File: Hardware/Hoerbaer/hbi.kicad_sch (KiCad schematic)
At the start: 49 parts, among them J6 PAW_A, J7 PAW_B, J8 PAW_C, J9 PAW_D, U2 PCF8574APWR, U3 PCF8574APWR, U4 PCF8574APWR, U5 TLC59108xPW, U6 TLC59108xPW, U7 TLC59108xPW

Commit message: Many small corrections, changed connectors, ...
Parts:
- J6, J7, J8, J9: now not fitted
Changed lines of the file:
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@@
   )
   (symbol (lib_id "Connector_Generic:Conn_02x12_Odd_Even") (at 72.39 139.7 0) (unit 1)
-    (in_bom yes) (on_board yes) (dnp no)
+    (in_bom yes) (on_board yes) (dnp yes)
     (property "Reference" "J9" (at 73.66 121.92 0)
       (effects (font (size 1.27 1.27)))
@@
   )
   (symbol (lib_id "Connector_Generic:Conn_02x12_Odd_Even") (at 72.39 96.52 0) (unit 1)
-    (in_bom yes) (on_board yes) (dnp no)
+    (in_bom yes) (on_board yes) (dnp yes)
     (property "Reference" "J8" (at 73.66 78.74 0)
       (effects (font (size 1.27 1.27)))
@@
   )
   (symbol (lib_id "Connector_Generic:Conn_02x12_Odd_Even") (at 36.83 96.52 0) (unit 1)
-    (in_bom yes) (on_board yes) (dnp no)
+    (in_bom yes) (on_board yes) (dnp yes)
     (property "Reference" "J6" (at 38.1 78.74 0)
       (effects (font (size 1.27 1.27)))
@@
   )
   (symbol (lib_id "Connector_Generic:Conn_02x12_Odd_Even") (at 36.83 139.7 0) (unit 1)
-    (in_bom yes) (on_board yes) (dnp no)
+    (in_bom yes) (on_board yes) (dnp yes)
     (property "Reference" "J7" (at 38.1 121.92 0)
       (effects (font (size 1.27 1.27)))

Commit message: WIP new hw rev
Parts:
- renumbered C23 to C10, C6 to C11, C7 to C12, C8 to C13, C9 to C14, C10 to C15, C11 to C16, C22 to C7, C65 to C8, C24 to C9, J8 to J10, J9 to J11, J6 to J8, J7 to J9
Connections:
- net +12V renamed +9V
- net VCC renamed VCC_P

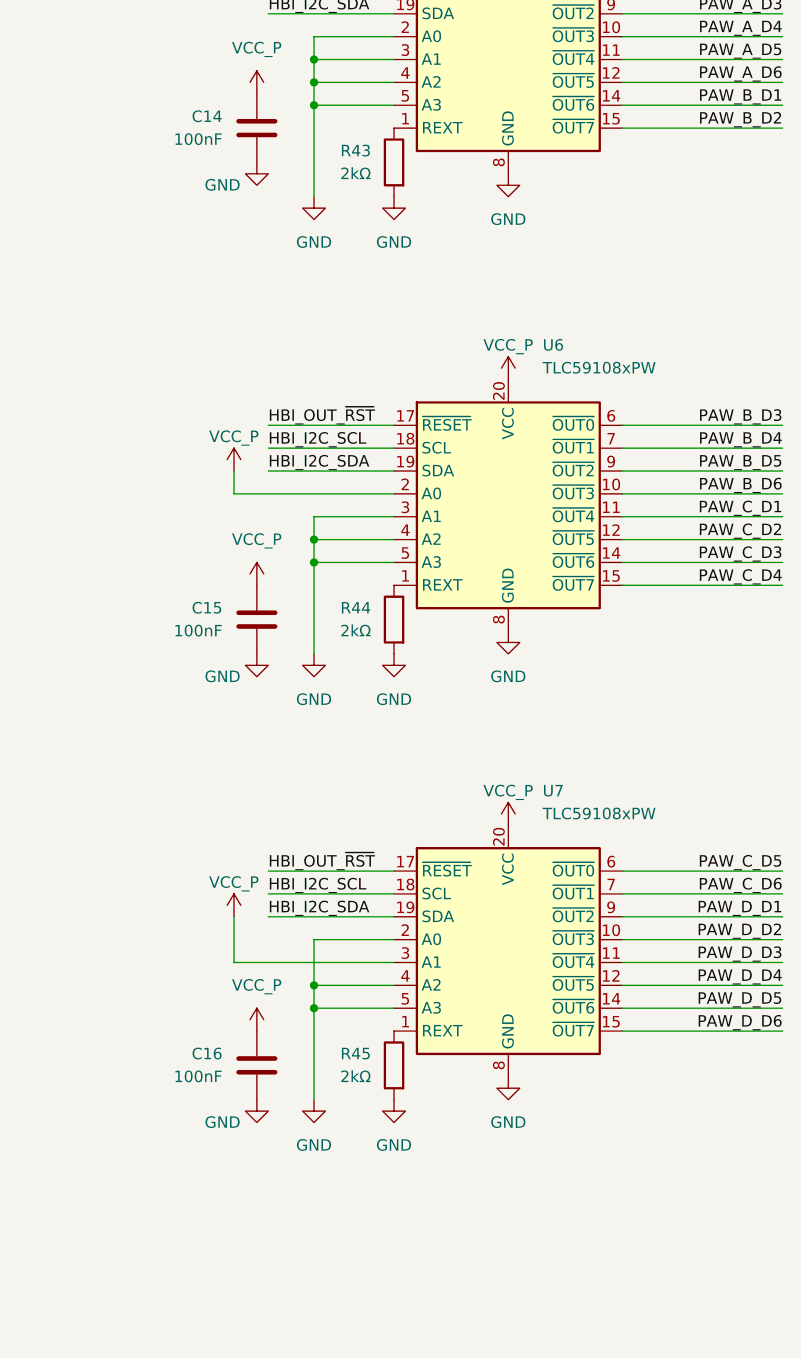
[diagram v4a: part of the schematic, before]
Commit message: Added more jumper options.
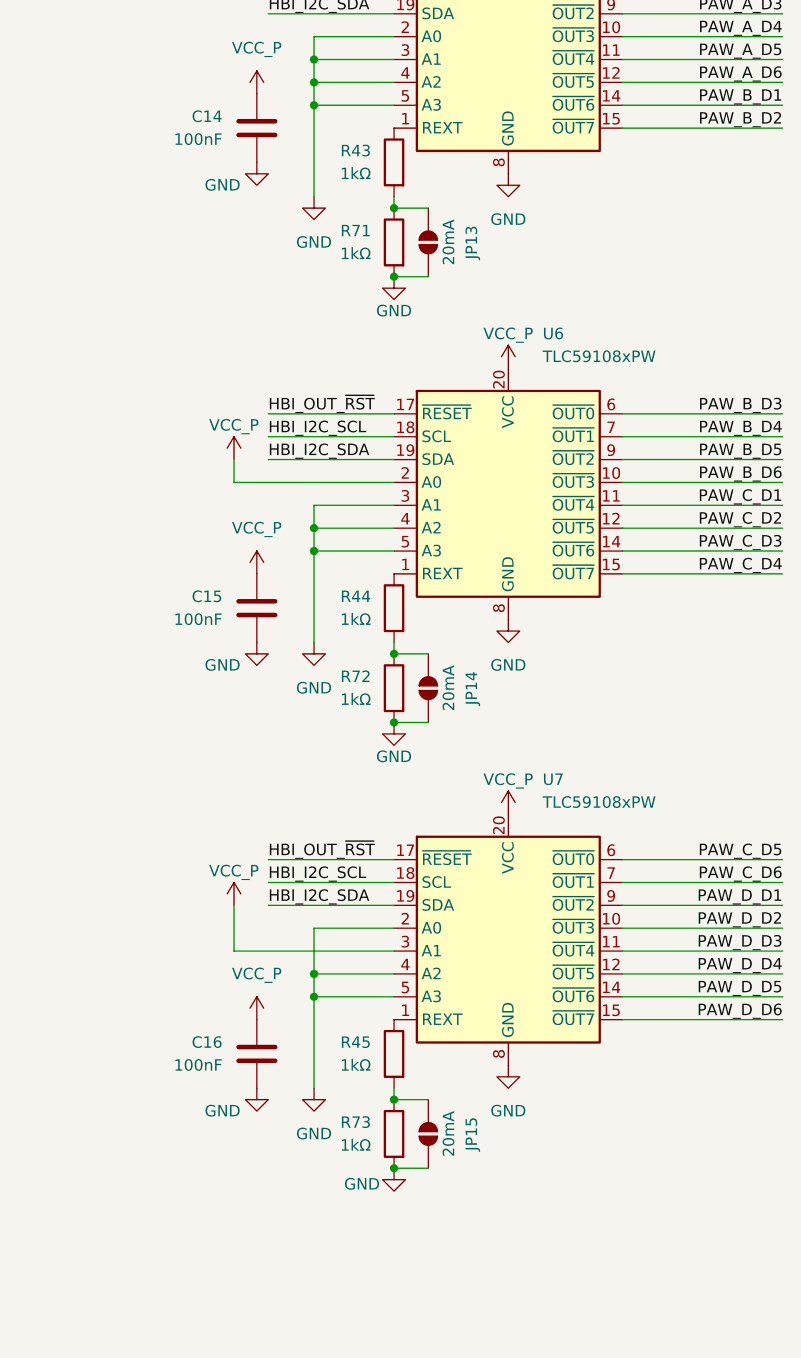
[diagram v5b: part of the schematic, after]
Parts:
- added JP13, JP14, JP15: 20mA, Jumper:SolderJumper-2_P1.3mm_Open_RoundedPad1.0x1.5mm, symbol Jumper:SolderJumper_2_Open
- added R71, R72, R73: 1kΩ, Resistor_SMD:R_0402_1005Metric, symbol Device:R
- R43, R44, R45: value 2kΩ -> 1kΩ; LCSC C4109 -> C11702; MPN 0402WGF2001TCE -> 0402WGF1001TCE
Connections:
- net GND: now also JP13.2 (B), JP14.2 (B), JP15.2 (B), R71.2, R72.2, R73.2; no longer R43.2, R44.2, R45.2
- new net: JP14.1 (A), R44.2, R72.1
- new net: JP13.1 (A), R43.2, R71.1
- new net: JP15.1 (A), R45.2, R73.1
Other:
- moved on the sheet: C15, C16, U6, U7

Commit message: BOM FIxes
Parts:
- C11, C12, C13, C14, C15, C16: LCSC C458949 -> C1525; MPN MT15B104K160CT -> CL05B104KO5NNNC
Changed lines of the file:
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@@
 			"L0RvY3VtZW50RGVsaXZlcnkvRERFQ29udHJvbGxlcj9BY3Rpb249c3JjaHJ0cnYmRG9jTm09ODI2"
 			"NTc2JkRvY1R5cGU9Q3VzdG9tZXIrRHJhd2luZyZEb2NMYW5nPUVuZ2xpc2gpLCBnZW5lcmF0ZWQg"
-			"d2l0aCBraWNhZC1mb290cA=="
+			"d2l0aCBraWNhZC1mb290cEggcGl0Y2ggMy41bW0gc2l6ZSA1Nng3LjZtbSBkcmlsbCAxLjJtbSBw"
+			"YWQgMi40bW0KMAoxNgoxNgpUZXJtaW5hbEJsb2NrX1Bob2VuaXgKVGVybWluYWxCbG9ja19QaG9l"
+			"bml4X1BULTEsNS0xNi01LjAtSF8xeDE2X1A1LjAwbW1fSG9yaXpvbnRhbApUZXJtaW5hbCBCbG9j"
+			"ayBQaG9lbml4IFBULTEsNS0xNi01LjAtSCwgMTYgcGlucywgcGl0Y2ggNW1tLCBzaXplIDgweDlt"
+			"bSwgZHJpbGwgZGlhbWV0ZXIgMS4zbW0sIHBhZCBkaWFtZXRlciAyLjZtbSwgaHR0cDovL3d3dy5t"
+			"b3VzZXIuY29tL2RzLzIvMzI0L0l0ZW1EZXRhaWxfMTkzNTE2MS05MjI1NzgucGRmLCBzY3JpcHQt"
+			"Z2VuZXJhdGVkIHVzaW5nIGh0dHBzOi8vZ2l0bGFiLmNvbS9raWNhZC9saWJyYXJpZXMva2ljYWQt"
+			"Zm9vdHByaW50LWdlbmVyYXRvci8tL3RyZWUvbWFzdGVyL3NjcmlwdHMvVGVybWluYWxCbG9ja19Q"
+			"aG9lbml4ClRIVCBUZXJtaW5hbCBCbG9jayBQaG9lbml4IFBULTEsNS0xNi01LjAtSCBwaXRjaCA1"
+			"bW0gc2l6ZSA4MHg5bW0gZHJpbGwgMS4zbW0gcGFkIDIuNm1tCjAKMTYKMTYKVGVybWluYWxCbG9j"
+			"a19QaG9lbml4ClRlcm1pbmFsQmxvY2tfUGhvZW5peF9QVFNNLTAsNS0yLTIsNS1WLVNNRF8xeDAy"
+			"LTFNUF9QMi41MG1tX1ZlcnRpY2FsClBob2VuaXhDb250YWN0IFBUU00wLDUgMiAyLDVtbSB2ZXJ0"
+			"aWNhbCBTTUQgc3ByaW5nIGNsYW1wIHRlcm1pbmFsIGJsb2NrIGNvbm5lY3RvciBodHRwOi8vd3d3"
+			"LnBob2VuaXhjb250YWN0LmNvbS91cy9wcm9kdWN0cy8xODE0NzAyL3BkZgpQaG9lbml4Q29udGFj"
+			"dCBQVFNNMC41IDIgMi41bW0gdmVydGljYWwgU01EIHNwcmluZyBjbGFtcCB0ZXJtaW5hbCBibG9j"
+			"ayBjb25uZWN0b3IgCjAKNAozClRlcm1pbmFsQmxvY2tfUGhvZW5peApUZXJtaW5hbEJsb2NrX1Bo"
+			"b2VuaXhfUFRTTS0wLDUtMi0yLjUtSC1USFJfMXgwMl9QMi41MG1tX0hvcml6b250YWwKVGVybWlu"
+			"YWwgQmxvY2sgUGhvZW5peCBQVFNNLTAsNS0yLTIuNS1ILVRIUiwgMiBwaW5zLCBwaXRjaCAyLjVt"
+			"bSwgc2l6ZSA3LjJ4MTBtbQ=="
 		)
 	)
@@
 			)
 		)
-		(property "LCSC" "C458949"
+		(property "LCSC" "C1525"
 			(at 99.06 110.49 0)
 			(effects
@@
 			)
 		)
-		(property "MPN" "MT15B104K160CT"
+		(property "MPN" "CL05B104KO5NNNC"
 			(at 99.06 110.49 0)
 			(effects
@@
 			)
 		)
-		(property "LCSC" "C458949"
+		(property "LCSC" "C1525"
 			(at 214.63 46.99 0)
 			(effects
@@
 			)
 		)
-		(property "MPN" "MT15B104K160CT"
+		(property "MPN" "CL05B104KO5NNNC"
 			(at 214.63 46.99 0)
 			(effects
@@
 			)
 		)
-		(property "LCSC" "C458949"
+		(property "LCSC" "C1525"
 			(at 99.06 48.26 0)
 			(effects
@@
 			)
 		)
-		(property "MPN" "MT15B104K160CT"
+		(property "MPN" "CL05B104KO5NNNC"
 			(at 99.06 48.26 0)
 			(effects
@@
 			)
 		)
-		(property "LCSC" "C458949"
+		(property "LCSC" "C1525"
 			(at 214.63 149.86 0)
 			(effects
@@
 			)
 		)
-		(property "MPN" "MT15B104K160CT"
+		(property "MPN" "CL05B104KO5NNNC"
 			(at 214.63 149.86 0)
 			(effects
@@
 			)
 		)
-		(property "LCSC" "C458949"
+		(property "LCSC" "C1525"
 			(at 99.06 170.18 0)
 			(effects
@@
 			)
 		)
-		(property "MPN" "MT15B104K160CT"
+		(property "MPN" "CL05B104KO5NNNC"
 			(at 99.06 170.18 0)
 			(effects
@@
 			)
 		)
-		(property "LCSC" "C458949"
+		(property "LCSC" "C1525"
 			(at 214.63 100.33 0)
 			(effects
@@
 			)
 		)
-		(property "MPN" "MT15B104K160CT"
+		(property "MPN" "CL05B104KO5NNNC"
 			(at 214.63 100.33 0)
 			(effects

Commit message: Production
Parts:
- J10, J11, J8, J9: FT Rotation Offset (none) -> 90; JLCPCB Rotation Offset 90 -> (none)
- U2, U3, U4, U5, U6, U7: JLCPCB Rotation Offset 90 -> (none)
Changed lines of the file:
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@@
 			"b2VuaXhfUFRTTS0wLDUtMi0yLjUtSC1USFJfMXgwMl9QMi41MG1tX0hvcml6b250YWwKVGVybWlu"
 			"YWwgQmxvY2sgUGhvZW5peCBQVFNNLTAsNS0yLTIuNS1ILVRIUiwgMiBwaW5zLCBwaXRjaCAyLjVt"
-			"bSwgc2l6ZSA3LjJ4MTBtbQ=="
+			"bSwgc2l6ZSA3LjJ4MTBtbf//////////////////////////////////////////////////////"
+			"////////////////////////////////////////////////////////////////////////////"
+			"////////////////////////////////////////////////////////////////////////////"
+			"////////////////////////////////////////////////////////////////////////////"
+			"////////////////////////////////////////////////////////////////////////////"
+			"////////////////////////////////////////////////////////////////////////////"
+			"////////////////////////////////////////////////////////////////////////////"
+			"////////////////////////////////////////////////////////////////////////////"
+			"////////////////////////////////////////////////////////////////////////////"
+			"////////////////////////////////////////////////////////////////////////////"
+			"////////////////////////////////////////////////////////////////////////////"
+			"////////////////////////////////////////////////////////////////////////////"
+			"////////////////////////////////////////////////////////////////////////////"
+			"////////////////////////////////////////////////////////////////////////////"
+			"////////////////////////////////////////////////////////////////////////////"
+			"////////////////////////////////////////////////////////////////////////////"
+			"////////////////////////////////////////////////////////////////////////////"
+			"////////////////////////////////////////////////////////////////////////////"
+			"/////////////////////4guiC6ILoguiC6ILoguiC6ILoguiC6ILoguiC6ILoguiC6ILoguiC6I"
+			"LoguiC6ILoguiC6ILoguiC6ILoguiC6ILoguiC6ILoguiC6ILoguiC6ILoguiC6ILoguiC6ILogu"
+			"iC6ILoguiC6ILoguiC6ILoguiC6ILoguiC6ILoguiC6ILoguiC6ILoguiC6ILoguiC6ILoguiC6I"
+			"LoguiC6ILoguiC6ILoguiC6ILoguiC6ILoguiC6ILoguiC6ILoguiC6ILoguiC6ILoguiC6ILogu"
+			"iC6ILoguiC6ILoguiC6ILoguiC6ILoguiC6ILoguiC6ILoguiC6ILoguiC6ILoguiC6ILoguiC6I"
+			"LoguiC6ILoguiC6ILoguiC6ILoguiC6ILoguiC6ILoguiC6ILoguiC6ILoguiC6ILoguiC6ILogu"
+			"iC6ILoguiC6ILoguiC6ILoguiC6ILoguiC6ILoguiC6ILoguiC6ILoguiC6ILoguiC6ILoguiC6I"
+			"LoguiC6ILoguiC6ILoguiC6ILoguiC6ILoguiC6ILoguiC6ILoguiC6ILoguiC6ILoguiC6ILogu"
+			"iC6ILoguiC6ILoguiC6ILoguiC6ILoguiC6ILoguiC6ILoguiC6ILoguiC6ILoguiC6ILoguiC6I"
+			"LoguiC6ILoguiC6ILoguiC6ILoguiC6ILoguiC6ILoguiC6ILoguiC6ILoguiC6ILoguiC6ILogu"
+			"iC6ILoguiC6ILoguiC6ILoguiC6ILoguiC6ILoguiC6ILoguiC6ILoguiC6ILoguiC6ILoguiC6I"
+			"LoguiC6ILoguiC6ILoguiC6ILoguiC6ILoguiC6ILoguiC6ILoguiC6ILoguiC6ILoguiC6ILogu"
+			"iC6ILoguiC6ILoguiC6ILoguiC6ILoguiC6ILoguiC6ILoguiC6ILoguiC6ILoguiC6ILoguiC6I"
+			"LoguiC6ILoguiC6ILoguiC6ILoguiC6ILoguiC6ILoguiC6ILoguiC6ILoguiC6ILoguiC6ILogu"
+			"iC6ILoguiC6ILoguiC6ILoguiC6ILoguiC6ILoguiC6ILoguiC6ILoguiC6ILoguiC6ILoguiC6I"
+			"LoguiC6ILoguiC6ILoguiC6ILoguiC6ILoguiC6ILoguiC6ILoguiC6ILoguiC6ILoguiC6ILogu"
+			"iC6ILoguiC6ILoguiC6ILoguiC6ILoguiC6ILoguiC6ILoguiC6ILoguiC6ILoguiC6ILoguiC6I"
+			"LoguiC6ILoguiC6ILoguiC6ILoguiC6ILoguiC6ILoguiC6ILoguiC6ILoguiC6ILoguiC6ILogu"
+			"iC6ILoguiC6ILoguiC6ILgAAAAAAAAAAAAAAAAAAAAAAAAAAAAAAAAAAAAAAAAAAAAAAAAAAAAAA"
+			"AAAAAAAAAAAAAAAAAAAAAAAAAAAAAAAAAAAAAAAAAAAAAAAAAAAAAAAAAAAAAAAAAAAAAAAAAAAA"
+			"AAAAAAAAAAAAAAAAAAAAAAAAAAAAAAAAAAAAAAAAAAAAAAAAAAAAAAAAAAAAAAAAAAAAAAAAAAAA"
+			"AAAAAAAAAAAAAAAAAAAAAAAAAAAAAAAAAAAAAAAAAAAAAAAAAAAAAAAAAAAAAAAAAAAAAAAAAAAA"
+			"AAAAAAAAAAAAAAAAAAAAAAAAAAAAAAAAAAAAAAAAAAAAAAAAAAAAAAAAAAAAAAAAAAAAAAAAAAAA"
+			"AAAAAAAAAAAAAAAAAAAAAAAAAAAAAAAAAAAAAAAAAAAAAAAAAAAAAAAAAAAAAAAAAAAAAAAAAAAA"
+			"AAAAAAAAAAAAAAAAAAAAAAAAAAAAAAAAAAAAAAAAAAAAAAAAAAAAAAAAAAAAAAAAAAAAAAAAAAAA"
+			"AAAAAAAAAAAAAAAAAAAAAAAAAAAAAAAAAAAAAAAAAAAAAAAAAAAAAAAAAAAAAAAAAAAAAAAAAAAA"
+			"AAAAAAAAAAAAAAAAAAAAAAAAAAAAAAAAAAAAAAAAAAAAAAAAAAAAAAAAAAAAAAAAAAAAAAAAAAAA"
+			"AAAAAAAAAAAAAAAAAAAAAAAAAAAAAAAAAAAAAAAAAAAAAAAAAAAAAAAAAAAAAAAAAAAAAAAAAAAA"
+			"AAAAAAAAAAAAAAAAAAAAAAAAAAAAAAAAAAAAAAAAAAAAAAAAAAAAAAAAAAAAAAAAAAAAAAAAAAAA"
+			"AAAAAAAAAAAAAAAAAAAAAAAAAAAAAAAAAAAAAAAAAAAAAAAAAAAAAAAAAAAAAAAAAAAAAAAAAAAA"
+			"AAAAAAAAAAAAAAAAAAAAAAAAAAAAAAAAAAAAAAAAAAAAAAAAAAAAAAAAAAAAAAAAAAAAAAAAAAAA"
+			"AAAAAAAAAAAAAAAAAAAAAAAAAAAAAAAAAAAAAAAAAAAAAAAAAAAAAAAAAAAAAAAAAAAAAAAAAAAA"
+			"AAAAAAAAAAAAAAAAAAAAAAAAAAAAAAAAAAAAAAAAAAAAAAAAAAAAAAAAAAAAAAAAAAAAAAAAAAAA"
+			"AAAAAAAAAAAAAAAAAAAAAAAAAAAAAAAAAAAAAAAAAAAAAAAAAAAAAAAAAAAAAAAAAAAAAAAAAAAA"
+			"AAAAAAAAAAAAAAAAAAAAAAAAAAAAAAAAAAAAAAAAAAAAAAAAAAAAAAAAAAAAAAAAAAAAAAAAAAAA"
+			"AAAAAAAAAAAAAAAAAAAAAAAAAAAAAAAAAAAAAAAAAAAAAAAAAAAAAAAAAAAAAAAAAAAAAAAAAAAA"
+			"AAAAAAAAAAAAAAAAAAAAAA=="
 		)
 	)
@@
 			)
 		)
-		(property "JLCPCB Rotation Offset" "90"
-			(at 130.81 172.72 0)
-			(effects
-				(font
-					(size 1.27 1.27)
-				)
-				(hide yes)
-			)
-		)
 		(property "Check_prices" ""
 			(at 130.81 172.72 0)
@@
 			)
 		)
+		(property "FT Rotation Offset" ""
+			(at 130.81 172.72 0)
+			(effects
+				(font
+					(size 1.27 1.27)
+				)
+			)
+		)
 		(pin "1"
 		)
@@
 			)
 		)
-		(property "JLCPCB Rotation Offset" "90"
-			(at 72.39 139.7 0)
-			(effects
-				(font
-					(size 1.27 1.27)
-				)
-				(hide yes)
-			)
-		)
 		(property "Check_prices" ""
 			(at 72.39 139.7 0)
@@
 			)
 		)
+		(property "FT Rotation Offset" "90"
+			(at 72.39 139.7 0)
+			(effects
+				(font
+					(size 1.27 1.27)
+				)
+			)
+		)
 		(pin "1"
 		)
@@
 			)
 		)
-		(property "JLCPCB Rotation Offset" "90"
-			(at 72.39 96.52 0)
-			(effects
-				(font
-					(size 1.27 1.27)
-				)
-				(hide yes)
-			)
-		)
 		(property "Check_prices" ""
 			(at 72.39 96.52 0)
@@
 			)
 		)
+		(property "FT Rotation Offset" "90"
+			(at 72.39 96.52 0)
+			(effects
+				(font
+					(size 1.27 1.27)
+				)
+			)
+		)
 		(pin "1"
 		)
@@
 			)
 		)
-		(property "JLCPCB Rotation Offset" "90"
-			(at 130.81 113.03 0)
-			(effects
-				(font
-					(size 1.27 1.27)
-				)
-				(hide yes)
-			)
-		)
 		(property "Check_prices" ""
 			(at 130.81 113.03 0)
@@
 			)
 		)
+		(property "FT Rotation Offset" ""
+			(at 130.81 113.03 0)
+			(effects
+				(font
+					(size 1.27 1.27)
+				)
+			)
+		)
 		(pin "1"
 		)
@@
 			)
 		)
-		(property "JLCPCB Rotation Offset" "90"
-			(at 242.57 138.43 0)
-			(effects
-				(font
-					(size 1.27 1.27)
-				)
-				(hide yes)
-			)
-		)
 		(property "Check_prices" ""
 			(at 242.57 138.43 0)
@@
 			)
 		)
+		(property "FT Rotation Offset" ""
+			(at 242.57 138.43 0)
+			(effects
+				(font
+					(size 1.27 1.27)
+				)
+			)
+		)
 		(pin "1"
 		)
@@
 			)
 		)
-		(property "JLCPCB Rotation Offset" "90"
-			(at 36.83 96.52 0)
-			(effects
-				(font
-					(size 1.27 1.27)
-				)
-				(hide yes)
-			)
-		)
 		(property "Check_prices" ""
 			(at 36.83 96.52 0)
@@
 			)
 		)
+		(property "FT Rotation Offset" "90"
+			(at 36.83 96.52 0)
+			(effects
+				(font
+					(size 1.27 1.27)
+				)
+			)
+		)
 		(pin "1"
 		)
@@
 			)
 		)
-		(property "JLCPCB Rotation Offset" "90"
-			(at 242.57 39.37 0)
-			(effects
-				(font
-					(size 1.27 1.27)
-				)
-				(hide yes)
-			)
-		)
 		(property "Check_prices" ""
 			(at 242.57 39.37 0)
@@
 			)
 		)
+		(property "FT Rotation Offset" ""
+			(at 242.57 39.37 0)
+			(effects
+				(font
+					(size 1.27 1.27)
+				)
+			)
+		)
 		(pin "1"
 		)
@@
 			)
 		)
-		(property "JLCPCB Rotation Offset" "90"
-			(at 36.83 139.7 0)
-			(effects
-				(font
-					(size 1.27 1.27)
-				)
-				(hide yes)
-			)
-		)
 		(property "Check_prices" ""
 			(at 36.83 139.7 0)
@@
 			)
 		)
+		(property "FT Rotation Offset" "90"
+			(at 36.83 139.7 0)
+			(effects
+				(font
+					(size 1.27 1.27)
+				)
+			)
+		)
 		(pin "1"
 		)
@@
 			)
 		)
-		(property "JLCPCB Rotation Offset" "90"
-			(at 242.57 88.9 0)
-			(effects
-				(font
-					(size 1.27 1.27)
-				)
-				(hide yes)
-			)
-		)
 		(property "Check_prices" ""
 			(at 242.57 88.9 0)
@@
 			)
 		)
+		(property "FT Rotation Offset" ""
+			(at 242.57 88.9 0)
+			(effects
+				(font
+					(size 1.27 1.27)
+				)
+			)
+		)
 		(pin "1"
 		)
@@
 			)
 		)
-		(property "JLCPCB Rotation Offset" "90"
-			(at 130.81 50.8 0)
-			(effects
-				(font
-					(size 1.27 1.27)
-				)
-				(hide yes)
-			)
-		)
 		(property "Check_prices" ""
 			(at 130.81 50.8 0)
@@
 			(at 130.81 50.8 0)
 			(effects
+				(font
+					(size 1.27 1.27)
+				)
+			)
+		)
+		(property "FT Rotation Offset" ""
+			(at 130.81 50.8 0)
+			(effects
